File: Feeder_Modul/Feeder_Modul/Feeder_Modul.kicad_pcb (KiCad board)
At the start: 2 copper layers, 156.6 x 125.2 mm, 68 parts, among them J101 Conn_02x01, J102 Conn_01x06_Male, J103 Conn_02x01, J104 Conn_01x02_Male, J105 Conn_01x02_Male, J106 USB_A, J107 Conn_02x07_Odd_Even, Q101 BC847, SW101 SW_Push, SW102 SW_Push, SW103 SW_Push, SW104 SW_Push, SW105 SW_Push, U101 TPS560430, U102 STM32F105R8Tx, U103 SN65HVD230DR, U104 EE-SX1350_PCB, U105 DRV8835, Y101 48MHz

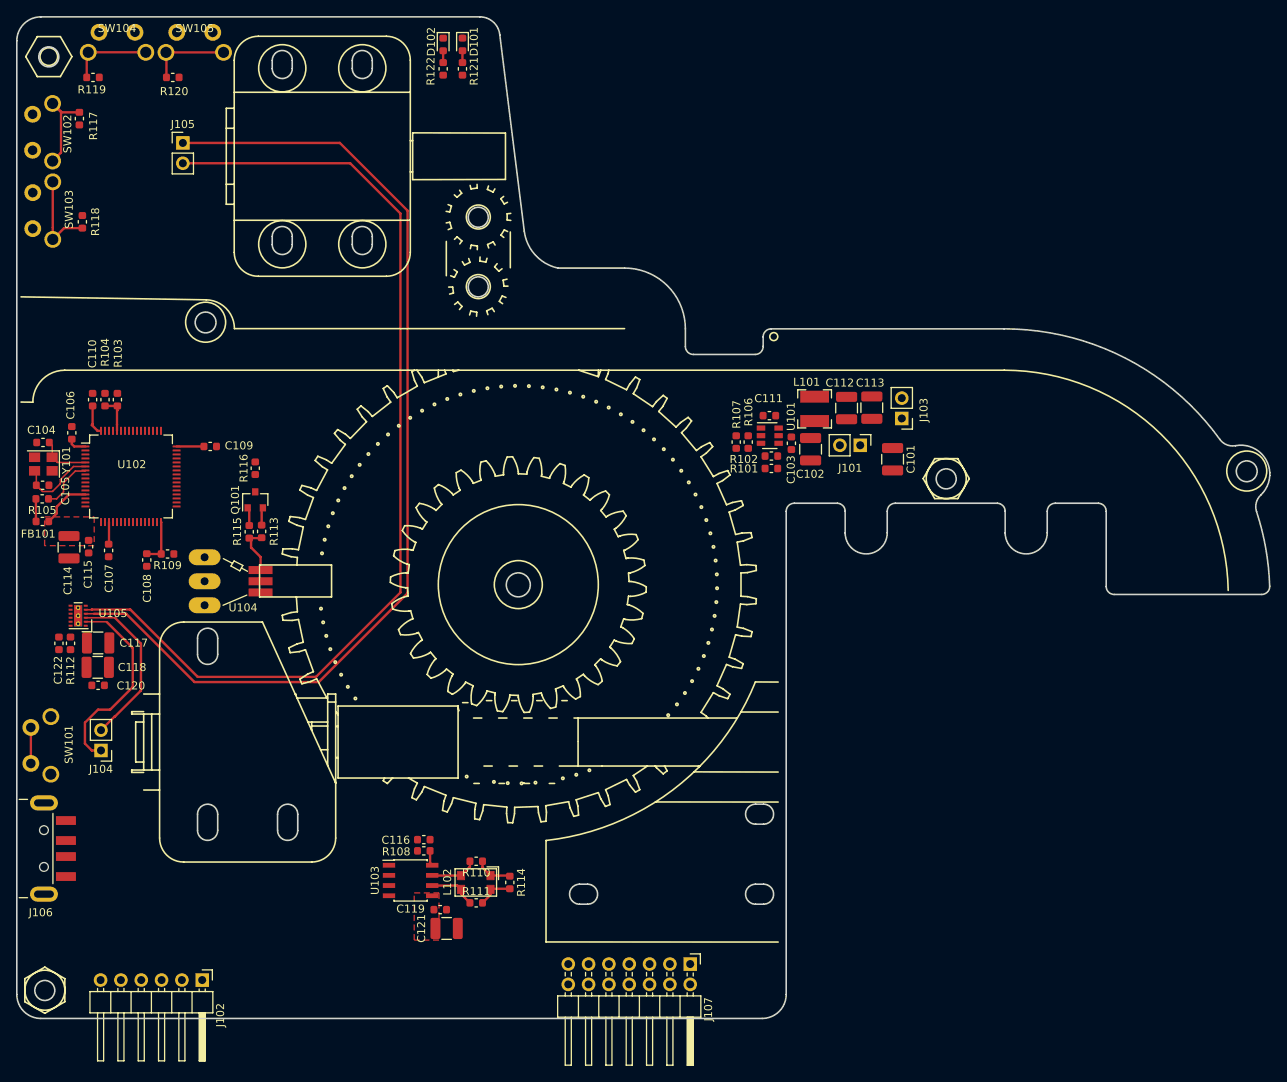
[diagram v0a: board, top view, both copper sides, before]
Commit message: PCB fast fertig geroutet, I2C EEPROM hinzugefügt
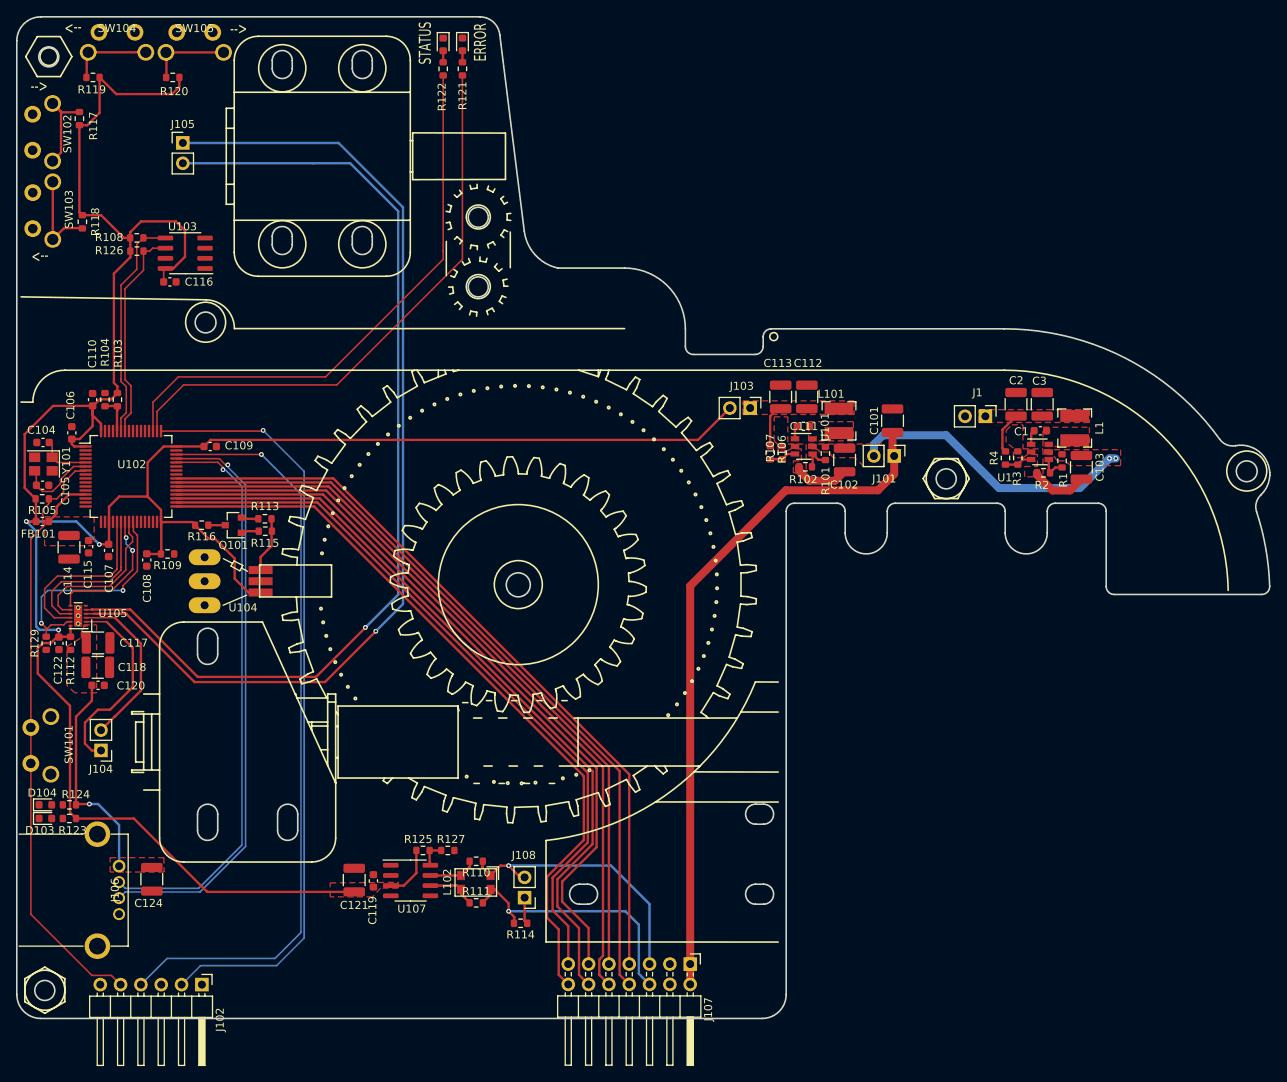
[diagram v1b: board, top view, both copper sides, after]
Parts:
- added C1: 100n 50V, Capacitor_SMD:C_0603_1608Metric, F.Cu at (191.8, 87.3)
- added C124: 10u 50V, Capacitor_SMD:C_1210_3225Metric, F.Cu at (80.7, 143.4)
- added C2: 10u 50V, Capacitor_SMD:C_1210_3225Metric, F.Cu at (188.7, 84.0)
- added C3: 10u 50V, Capacitor_SMD:C_1210_3225Metric, F.Cu at (192.0, 84.0)
- added D103: LED_Blue, LED_SMD:LED_0603_1608Metric, F.Cu at (67.4, 135.8)
- added D104: LED_Blue, LED_SMD:LED_0603_1608Metric, F.Cu at (67.4, 134.1)
- added J1: Conn_02x01, Connector_PinHeader_2.54mm:PinHeader_1x02_P2.54mm_Vertical, F.Cu at (184.9, 85.5)
- added J108: Conn_02x01, Connector_PinHeader_2.54mm:PinHeader_1x02_P2.54mm_Vertical, F.Cu at (127.3, 145.7)
- added L1: 12u SRN4018, Inductor_SMD:L_Bourns-SRN4018, F.Cu at (196.1, 87.0)
- added R1: 51K, Resistor_SMD:R_0603_1608Metric, F.Cu at (194.5, 91.1)
- added R123: 1k, Resistor_SMD:R_0603_1608Metric, F.Cu at (70.4, 135.8)
- added R124: 1k, Resistor_SMD:R_0603_1608Metric, F.Cu at (70.4, 134.1)
- added R125: DNP, Resistor_SMD:R_0603_1608Metric, F.Cu at (114.6, 139.8)
- added R126: 1k, Resistor_SMD:R_0603_1608Metric, F.Cu at (78.8, 64.9)
- added R127: 10K, Resistor_SMD:R_0603_1608Metric, F.Cu at (117.7, 139.8)
- added R129: 10K, Resistor_SMD:R_0603_1608Metric, F.Cu at (67.5, 113.9)
- added R2: 51K, Resistor_SMD:R_0603_1608Metric, F.Cu at (192.2, 92.6)
- added R3: 22K1, Resistor_SMD:R_0603_1608Metric, F.Cu at (188.9, 90.7)
- added R4: 88K7, Resistor_SMD:R_0603_1608Metric, F.Cu at (187.4, 90.7)
- added U1: TPS560430, Package_TO_SOT_SMD:SOT-23-6, F.Cu at (191.7, 90.0)
- added U107: SN65HVD230, Package_SO:SOIC-8_3.9x4.9mm_P1.27mm, F.Cu at (113.0, 143.6)
- C103: value 100n 50V -> 10u 50V; footprint Capacitor_SMD:C_0603_1608Metric -> Capacitor_SMD:C_1210_3225Metric
- C116, C119: value 100n -> 100n 50V
- C121: value 10u -> 10u 50V
- D101: value LED_Small -> LED_red
- D102: value LED_Small -> LED_green
- J104, J105: value Conn_01x02_Male -> Conn_02x01
- J106: footprint Connector_USB:USB_A_CNCTech_1001-011-01101_Horizontal -> ProjectFootprints:USB-A-Conn_LCSC
- R108: value 10K -> 1k
- R113, R116, R117, R118, R119, R120: value 10k -> 10K
- U103: value SN65HVD230DR -> M24C01-WMN
- moved R108 84.6 mm to (78.8, 63.2), turned to 180 degrees
- moved U103 83.3 mm to (84.9, 65.2), turned to 180 degrees
- moved C116 76.6 mm to (83.0, 68.7)
- moved C103 36.4 mm to (196.9, 91.9)
- moved J103 19.0 mm to (155.5, 84.5), turned to 270 degrees
- moved J106 17.1 mm to (76.6, 144.8), turned to 270 degrees
- moved C121 13.0 mm to (106.0, 143.5), turned to 90 degrees
- moved C113 11.5 mm to (159.3, 83.1)
- moved R116 9.77 mm to (86.9, 99.1), turned to 180 degrees
- moved C119 9.09 mm to (108.4, 143.6), turned to 90 degrees
- moved R101 7.00 mm to (164.9, 90.2), turned to 270 degrees
- moved R114 5.28 mm to (126.8, 148.9), turned to 180 degrees
- moved C112 5.16 mm to (162.6, 83.1)
- moved C101 4.82 mm to (173.3, 86.1), turned to 90 degrees
- moved C111 4.46 mm to (162.2, 86.8)
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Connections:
- net /PA11 renamed /USB_OTG-
- net /PA12 renamed /USB_OTG+
- J102 pad 6: (no net) -> Net-(J102-Pad6)
- J106 pad 1: (no net) -> +5V
- J107 pad 10: (no net) -> /ADDR3
- J107 pad 11: (no net) -> /ADDR4
- J107 pad 12: (no net) -> /ADDR5
- J107 pad 13: (no net) -> /ADDR6
- J107 pad 14: (no net) -> /ADDR7
- J107 pad 2: GND -> +24V
- J107 pad 3: +24V -> GND
- J107 pad 7: (no net) -> /ADDR0
- J107 pad 8: (no net) -> /ADDR1
- J107 pad 9: (no net) -> /ADDR2
- R108 pad 1: +3V3 -> /I2C1_SDA
- R108 pad 2: Net-(R108-Pad2) -> +3V3
- R114 pad 1: /CAN1_H -> Net-(J108-Pad1)
- R121 pad 2: (no net) -> /LED_error
- R122 pad 2: (no net) -> /LED_status
- U102 pad 10: (no net) -> Net-(U102-Pad10)
- U102 pad 11: (no net) -> Net-(U102-Pad11)
- U102 pad 14: (no net) -> Net-(U102-Pad14)
- U102 pad 15: (no net) -> Net-(U102-Pad15)
- U102 pad 16: (no net) -> Net-(U102-Pad16)
- U102 pad 17: (no net) -> Net-(U102-Pad17)
- U102 pad 2: (no net) -> Net-(U102-Pad2)
- U102 pad 20: (no net) -> Net-(U102-Pad20)
- U102 pad 21: (no net) -> /DIR_A
- U102 pad 22: (no net) -> /PA6
- U102 pad 23: (no net) -> /PA7
- U102 pad 24: (no net) -> /DIR_B
- U102 pad 25: (no net) -> /MODE
- U102 pad 26: (no net) -> Net-(U102-Pad26)
- U102 pad 27: (no net) -> Net-(U102-Pad27)
- U102 pad 28: (no net) -> Net-(U102-Pad28)
- U102 pad 29: (no net) -> Net-(U102-Pad29)
- U102 pad 3: (no net) -> Net-(U102-Pad3)
- U102 pad 30: (no net) -> Net-(U102-Pad30)
- U102 pad 33: (no net) -> /ADDR7
- U102 pad 34: (no net) -> /ADDR6
- U102 pad 35: (no net) -> /ADDR5
- U102 pad 36: (no net) -> /ADDR4
- U102 pad 37: (no net) -> /ADDR3
- U102 pad 38: (no net) -> /ADDR2
- U102 pad 39: (no net) -> /ADDR1
- U102 pad 4: (no net) -> Net-(U102-Pad4)
- U102 pad 40: (no net) -> /ADDR0
- U102 pad 41: (no net) -> /PA8
- U102 pad 42: (no net) -> +5V
- U102 pad 43: (no net) -> /PA10
- U102 pad 50: (no net) -> /LED_error
- U102 pad 51: (no net) -> /LED_status
- U102 pad 52: (no net) -> Net-(U102-Pad52)
- U102 pad 53: (no net) -> Net-(U102-Pad53)
- U102 pad 54: (no net) -> Net-(U102-Pad54)
- U102 pad 55: (no net) -> Net-(U102-Pad55)
- U102 pad 56: (no net) -> Net-(U102-Pad56)
- U102 pad 57: (no net) -> Net-(U102-Pad57)
- U102 pad 58: (no net) -> /I2C1_SCL
- U102 pad 59: (no net) -> /I2C1_SDA
- U102 pad 8: (no net) -> Net-(U102-Pad8)
- U102 pad 9: (no net) -> Net-(U102-Pad9)
- U103 pad 1: /CAN1_TX -> GND
- U103 pad 3: +3V3 -> GND
- U103 pad 4: /CAN1_RX -> GND
- U103 pad 5: +3V3 -> /I2C1_SDA
- U103 pad 6: Net-(L102-Pad3) -> /I2C1_SCL
- U103 pad 7: Net-(L102-Pad1) -> GND
- U103 pad 8: Net-(R108-Pad2) -> +3V3
- U104 pad 2: (no net) -> Net-(U104-Pad2)
- U104 pad 5: (no net) -> Net-(U104-Pad5)
- U105 pad 10: (no net) -> /DIR_A
- U105 pad 11: (no net) -> /MODE
- U105 pad 7: (no net) -> /PA7
- U105 pad 8: (no net) -> /DIR_B
- U105 pad 9: (no net) -> /PA6
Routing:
- net +3V3: track 21.2 -> 334.0 mm, vias 0 -> 3
- net /ADDR1: track 0.00 -> 97.5 mm
- net /ADDR5: track 0.00 -> 96.2 mm
- net /PA14: track 0.00 -> 96.1 mm, vias 0 -> 1
- net /ADDR0: track 0.00 -> 95.6 mm
- net /ADDR3: track 0.00 -> 95.5 mm
- net /PA13: track 0.00 -> 95.1 mm, vias 0 -> 1
- net /ADDR4: track 0.00 -> 94.3 mm
- net /ADDR7: track 0.00 -> 93.9 mm
- net /ADDR2: track 0.00 -> 93.2 mm
- net /ADDR6: track 0.00 -> 91.9 mm
- net +24V: track 0.00 -> 86.5 mm
- net /USB_OTG+: track 0.00 -> 73.9 mm, vias 0 -> 1
- net /USB_OTG-: track 0.00 -> 72.4 mm, vias 0 -> 1
- net /LED_error: track 0.00 -> 71.5 mm
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- added copper zone on F.Cu, net +5V
- added copper zone on F.Cu, net GND
- added copper zone on F.Cu, net Net-(C1-Pad1)
- added copper zone on F.Cu, net Net-(C102-Pad1)
- added copper zone on F.Cu, net Net-(C111-Pad1)
- added copper zone on F.Cu, net Net-(C112-Pad1)
- added copper zone on F.Cu, net Net-(C2-Pad1)
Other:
- board text added: "-->"
- board text added: "ERROR"
- board text added: "STATUS"

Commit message: Feeder fertig
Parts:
- added R128: 88K7, Resistor_SMD:R_0603_1608Metric, F.Cu at (118.1, 155.2)
- added R130: 88K7, Resistor_SMD:R_0603_1608Metric, F.Cu at (119.6, 155.2)
- added R131: 88K7, Resistor_SMD:R_0603_1608Metric, F.Cu at (121.1, 155.2)
- added R132: 88K7, Resistor_SMD:R_0603_1608Metric, F.Cu at (122.6, 155.2)
- added R133: 88K7, Resistor_SMD:R_0603_1608Metric, F.Cu at (124.1, 155.2)
- added R134: 88K7, Resistor_SMD:R_0603_1608Metric, F.Cu at (125.6, 155.2)
- added R135: 88K7, Resistor_SMD:R_0603_1608Metric, F.Cu at (127.1, 155.2)
- added R136: 88K7, Resistor_SMD:R_0603_1608Metric, F.Cu at (128.6, 155.2)
- R112: value 0R -> DNP
- moved R124 83.4 mm to (71.3, 50.8)
- moved D104 83.4 mm to (68.0, 50.8)
- moved R123 79.0 mm to (71.3, 56.9)
- moved D103 79.0 mm to (68.0, 56.9)
- moved R117 67.3 mm to (71.8, 115.6), turned to 0 degrees
- moved SW103 60.2 mm to (66.2, 120.0)
- moved SW102 59.8 mm to (66.2, 109.8)
- moved R118 57.3 mm to (71.8, 118.5), turned to 0 degrees
- moved SW101 44.3 mm to (96.0, 158.9), turned to 0 degrees
- moved R126 20.0 mm to (85.7, 83.7)
- moved R108 20.0 mm to (85.7, 82.0)
- moved U103 20.0 mm to (91.8, 84.0)
- moved C116 17.5 mm to (86.3, 85.9), turned to 180 degrees
- moved C117 5.10 mm to (79.0, 112.9)
- moved C118 5.10 mm to (78.9, 115.9)
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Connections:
- J102 pad 6: Net-(J102-Pad6) -> (no net)
- U102 pad 10: Net-(U102-Pad10) -> (no net)
- U102 pad 11: Net-(U102-Pad11) -> (no net)
- U102 pad 14: Net-(U102-Pad14) -> (no net)
- U102 pad 15: Net-(U102-Pad15) -> /BTN_TBACK
- U102 pad 16: Net-(U102-Pad16) -> /BTN_TFOR
- U102 pad 17: Net-(U102-Pad17) -> (no net)
- U102 pad 2: Net-(U102-Pad2) -> (no net)
- U102 pad 20: Net-(U102-Pad20) -> (no net)
- U102 pad 26: Net-(U102-Pad26) -> (no net)
- U102 pad 27: Net-(U102-Pad27) -> (no net)
- U102 pad 28: Net-(U102-Pad28) -> (no net)
- U102 pad 29: Net-(U102-Pad29) -> (no net)
- U102 pad 3: Net-(U102-Pad3) -> (no net)
- U102 pad 30: Net-(U102-Pad30) -> /ENC_OUT
- U102 pad 4: Net-(U102-Pad4) -> (no net)
- U102 pad 41: /PA8 -> (no net)
- U102 pad 43: /PA10 -> (no net)
- U102 pad 52: Net-(U102-Pad52) -> (no net)
- U102 pad 53: Net-(U102-Pad53) -> (no net)
- U102 pad 54: Net-(U102-Pad54) -> (no net)
- U102 pad 55: Net-(U102-Pad55) -> /BTN_SFOR
- U102 pad 56: Net-(U102-Pad56) -> /BTN_SBACK
- U102 pad 57: Net-(U102-Pad57) -> (no net)
- U102 pad 8: Net-(U102-Pad8) -> (no net)
- U102 pad 9: Net-(U102-Pad9) -> (no net)
- U104 pad 2: Net-(U104-Pad2) -> (no net)
- U104 pad 5: Net-(U104-Pad5) -> (no net)
- U107 pad 5: Net-(U107-Pad5) -> (no net)
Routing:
- net +5V: track 27.4 -> 255.9 mm, vias 1 -> 6
- net /CAN1_RX: track 0.00 -> 89.2 mm, vias 0 -> 2
- net /CAN1_TX: track 0.00 -> 86.5 mm, vias 0 -> 2
- net /BTN_SFOR: track 10.4 -> 59.2 mm, vias 0 -> 1
- net /BTN_SBACK: track 10.4 -> 58.4 mm, vias 0 -> 1
- net /ADDR0: track 95.6 -> 125.6 mm
- net +3V3: track 334.0 -> 361.6 mm
- net /BTN_TFOR: track 11.5 -> 38.2 mm, vias 0 -> 1
- net /ADDR2: track 93.2 -> 117.3 mm
- net /ADDR1: track 97.5 -> 121.3 mm
- net /NRST: track 74.5 -> 97.6 mm
- net /ADDR3: track 95.5 -> 113.6 mm
- net /ADDR4: track 94.3 -> 112.1 mm
- net /BTN_TBACK: track 11.9 -> 27.6 mm, vias 0 -> 1
- net /ADDR6: track 91.9 -> 103.5 mm
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- added copper zone on B.Cu, net GND
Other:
- board text added: "+3.3V"
- board text added: "+5V"
- board text added: "Feeder Modul V0.1"

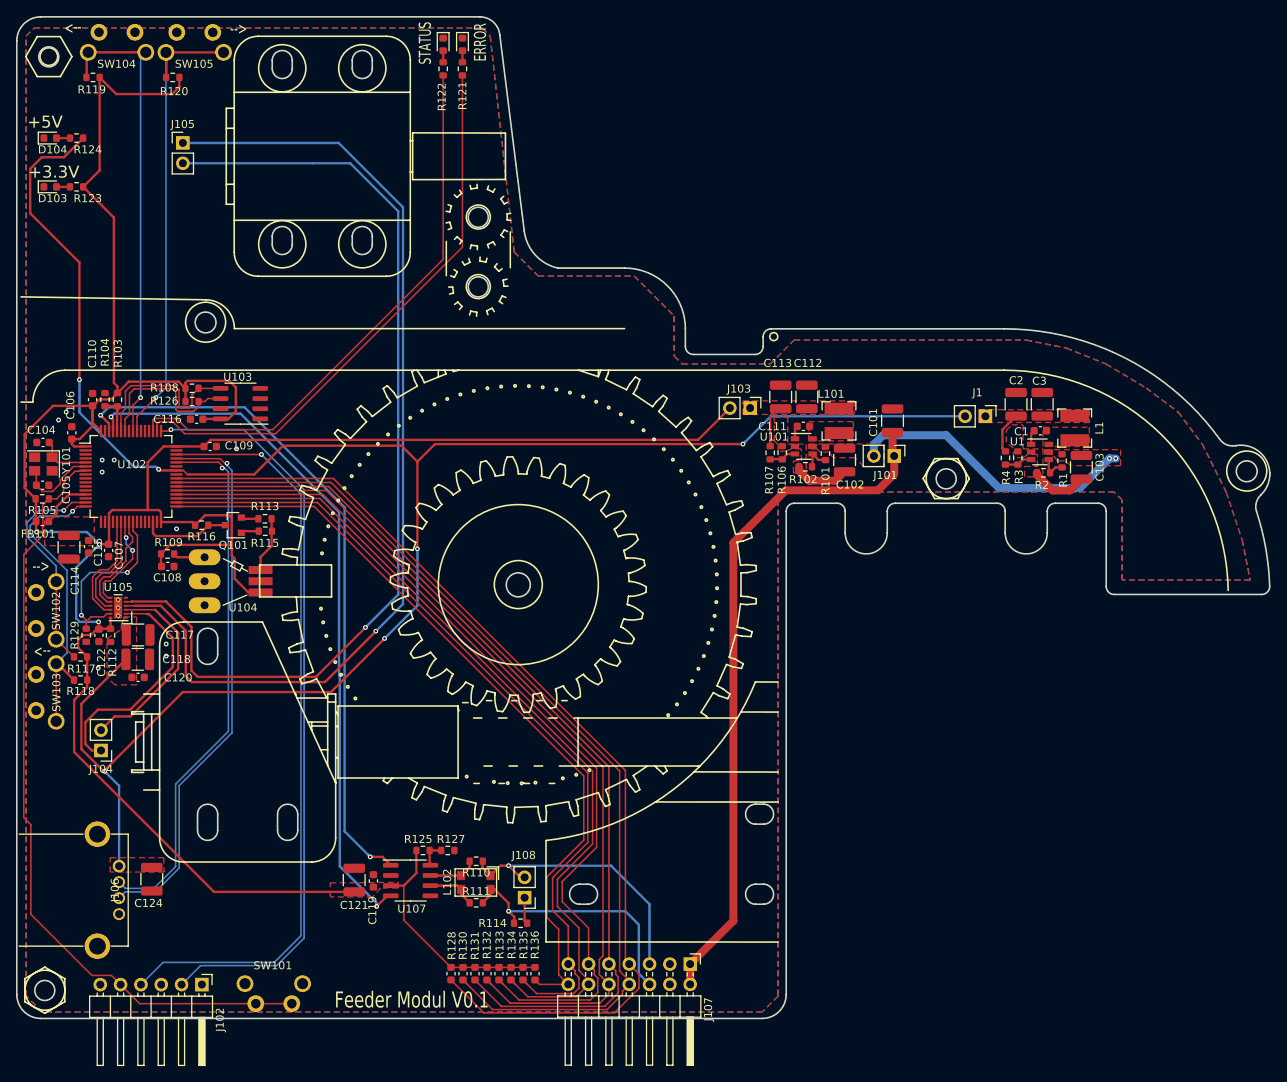
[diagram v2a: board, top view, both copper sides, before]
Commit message: Feeder Microswitch für Tape Motor hinzugefügt. Einige 3D Step Modelle hinzugefügt. Stepper Board die Ecken abgerundet.
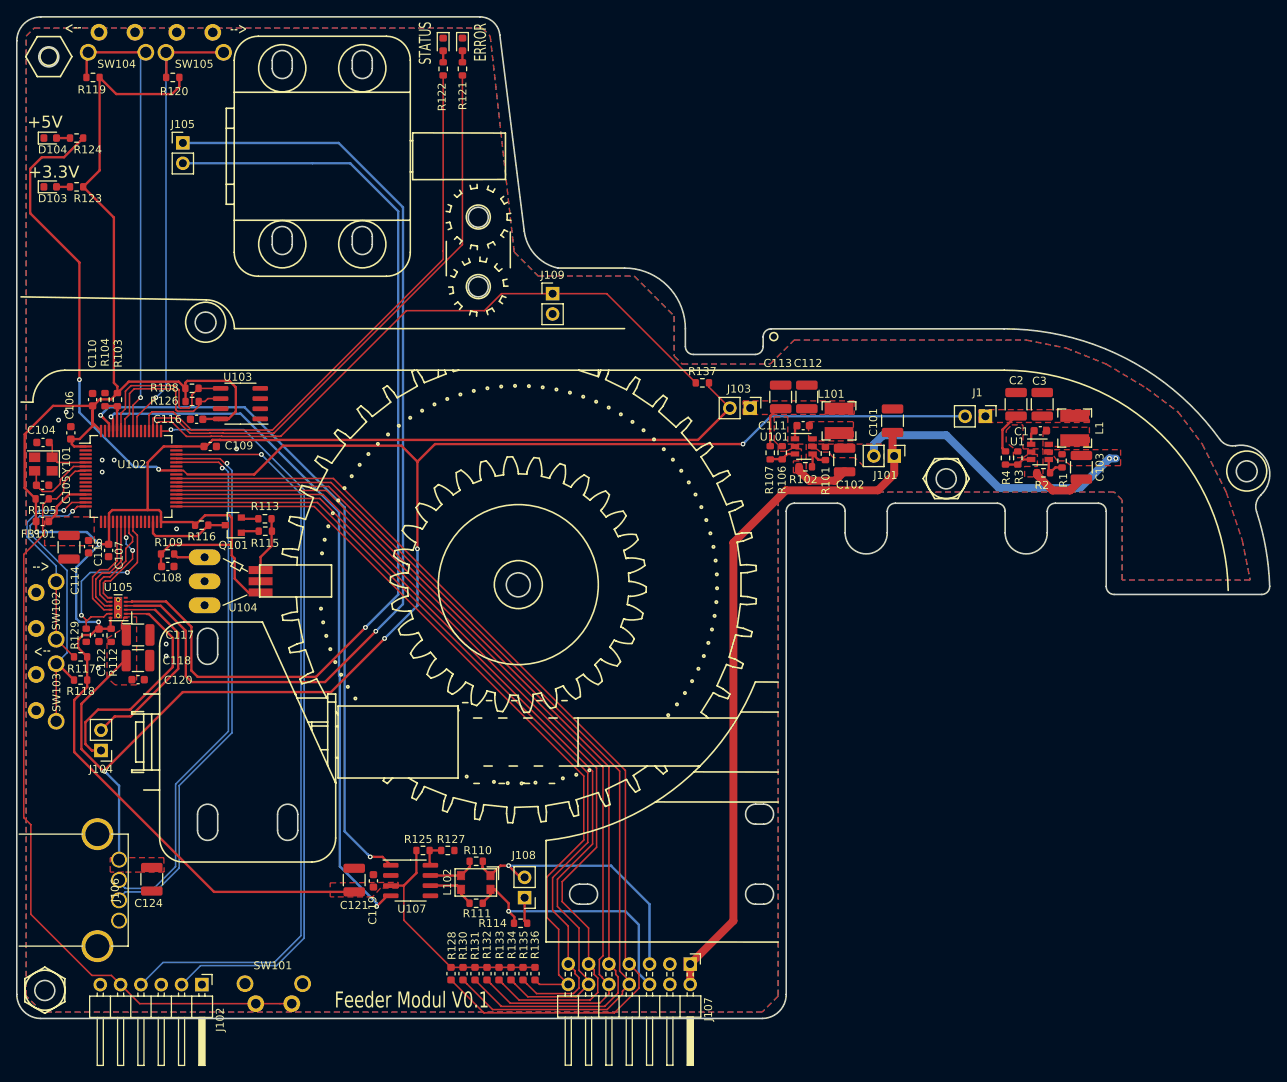
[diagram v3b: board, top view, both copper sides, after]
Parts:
- added J109: Conn_02x01, Connector_PinHeader_2.54mm:PinHeader_1x02_P2.54mm_Vertical, F.Cu at (130.8, 70.2)
- added R137: 10K, Resistor_SMD:R_0603_1608Metric, F.Cu at (149.5, 81.3)
- moved C120 0.29 mm to (79.0, 118.5)
- moved C118 0.16 mm to (79.0, 116.1)
- moved C106 0.12 mm to (70.6, 87.6)
- moved C111 0.09 mm to (162.1, 86.7)
- moved R112 0.08 mm to (75.6, 112.9)
- moved R111 0.05 mm to (121.2, 146.4)
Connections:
- U102 pad 50: /LED_error -> /TAPE_MICROBTN
- U102 pad 51: /LED_status -> /LED_error
- U102 pad 52: (no net) -> /LED_status
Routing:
- net /TAPE_MICROBTN: track 0.00 -> 81.2 mm
- net +3V3: track 361.6 -> 365.8 mm
- net /LED_status: track 70.3 -> 71.8 mm
- net /LED_error: track 70.9 -> 72.0 mm
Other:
- outline, holes or cut-outs redrawn
